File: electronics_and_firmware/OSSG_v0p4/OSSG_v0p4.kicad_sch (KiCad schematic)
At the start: 71 parts, among them IC1 DW01A, J1 USB_B_Micro, J2 External PDM Mic Input, Q1 FS8205A, Q2 Q_NPN_BEC, Q3 Q_NPN_BEC, Q4 Q_PMOS_GSD, SW1 SW_SPST, U1 ESP32-PICO-D4, U2 TP4056, U3 NCP167BMX330TBG, U4 CH9102F, U5 XC61CC3002MR, U6 MP23DB01HPTR

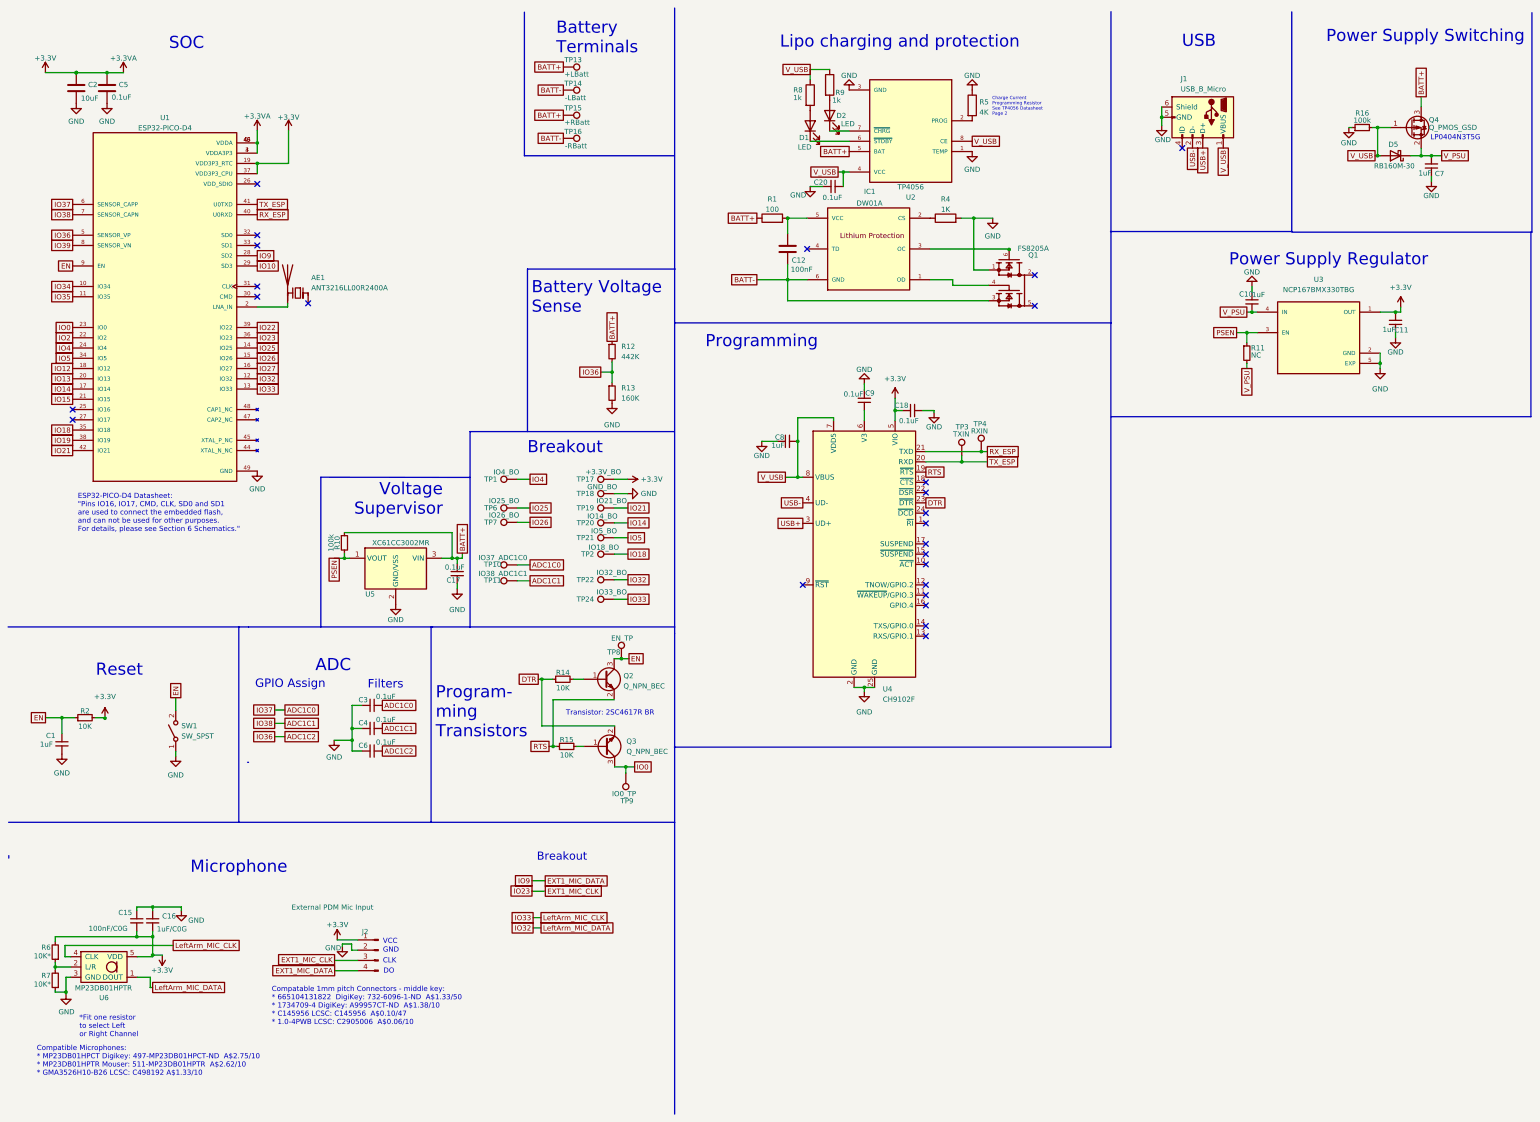
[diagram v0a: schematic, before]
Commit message: partial schematic update
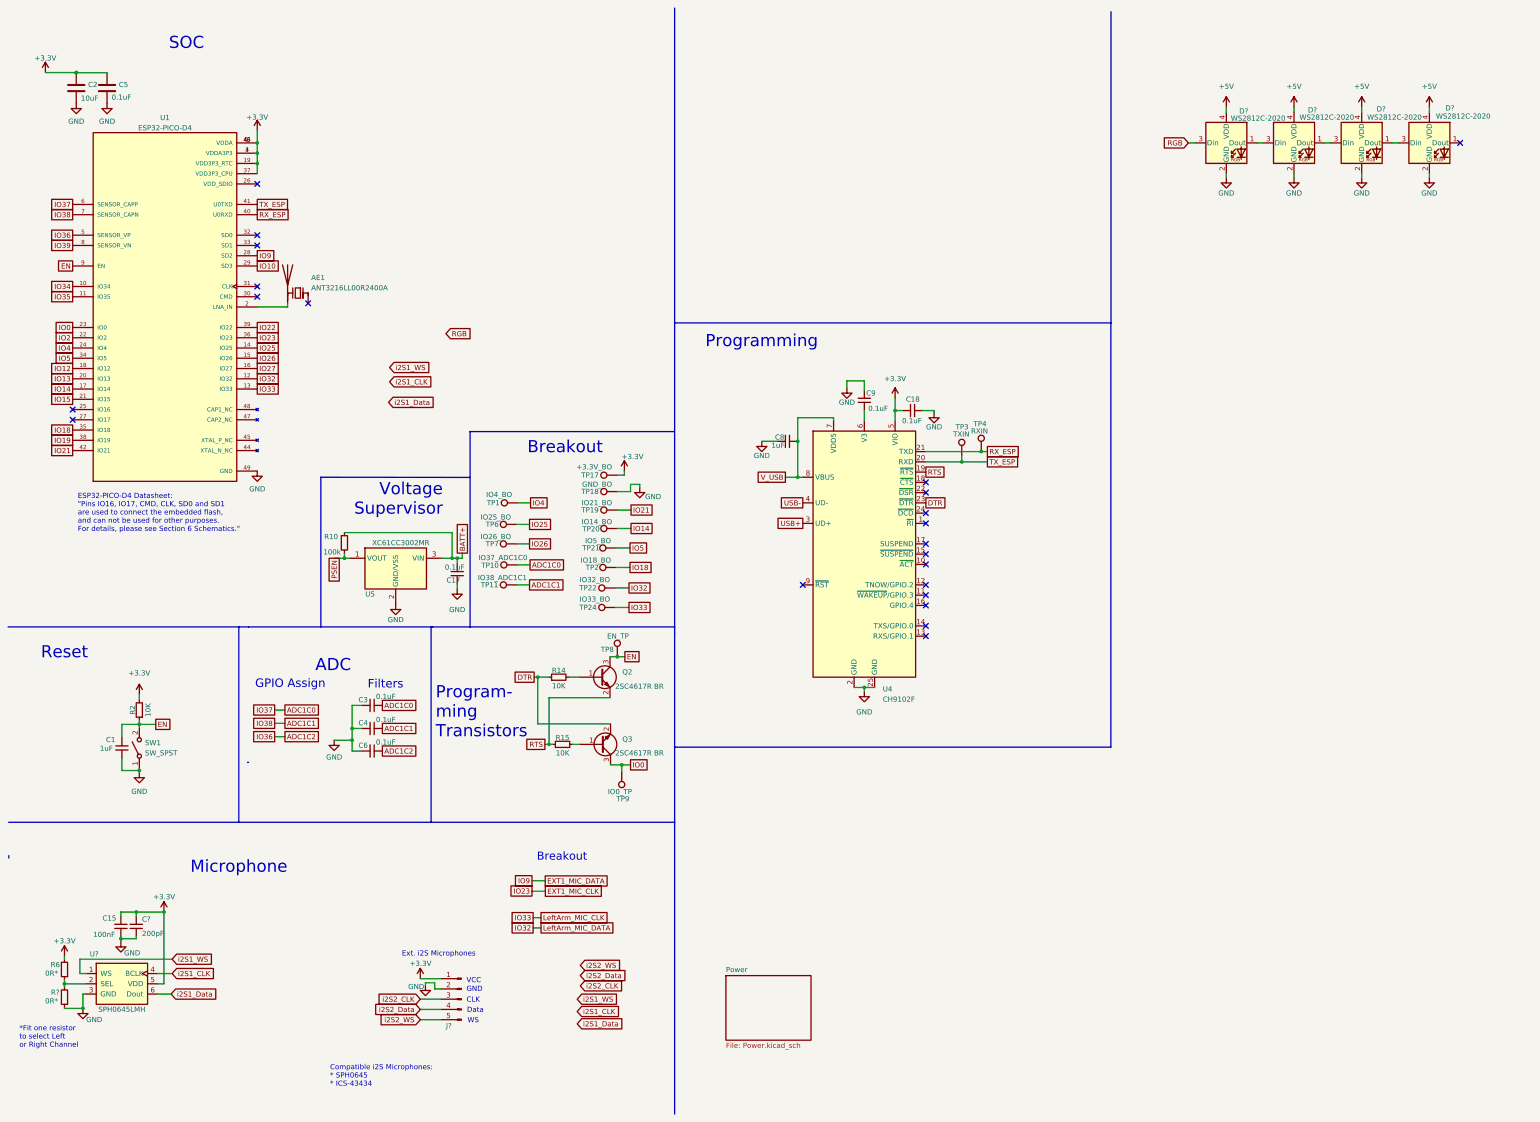
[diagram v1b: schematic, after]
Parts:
- removed C10, C11, C7: 1uF, Capacitor_SMD:C_0402_1005Metric, symbol Device:C_Small
- removed C12: 100nF, Capacitor_SMD:C_0402_1005Metric, symbol Device:C
- removed C16: 1uF/C0G, 1uF, symbol Device:C_Small
- removed C20: 0.1uF, Capacitor_SMD:C_0402_1005Metric, symbol Device:C_Small
- removed D1, D2: LED, Diode_SMD:D_0402_1005Metric, symbol Device:LED
- removed D5: RB160M-30, Diode_SMD:D_SOD-123, symbol Device:D_Schottky
- removed IC1: DW01A, Package_TO_SOT_SMD:SOT-23-6, symbol DW01A:DW01A
- removed J1: USB_B_Micro, Connector_USB:USB_Micro-B_Amphenol_10118194_Horizontal, symbol Connector:USB_B_Micro
- removed J2: External PDM Mic Input, OSSG_footprints:Solder-4P-Connector, symbol Connector:Conn_01x04_Male
- removed Q1: FS8205A, Package_TO_SOT_SMD:SOT-23-6, symbol FS8205A:FS8205A
- removed Q4: Q_PMOS_GSD, Package_TO_SOT_SMD:SOT-883, symbol Device:Q_PMOS_GSD
- removed R1: 100, Resistor_SMD:R_0402_1005Metric, symbol Device:R
- removed R11: NC, Resistor_SMD:R_0201_0603Metric, symbol Device:R_Small
- removed R12: 442K, Resistor_SMD:R_0402_1005Metric, symbol Device:R_Small
- removed R13: 160K, Resistor_SMD:R_0402_1005Metric, symbol Device:R_Small
- removed R16: 100k, Resistor_SMD:R_0402_1005Metric, symbol Device:R_Small
- removed R4: 1K, Resistor_SMD:R_0402_1005Metric, symbol Device:R
- removed R5: 4K, Resistor_SMD:R_0402_1005Metric, symbol Device:R
- removed R7: 10K*, Resistor_SMD:R_0402_1005Metric, symbol Device:R_Small
- removed R8, R9: 1k, Resistor_SMD:R_0402_1005Metric, symbol Device:R
- removed TP13: +LBatt, OSSG_footprints:Breakout_pads, symbol Connector:TestPoint
- removed TP14: -LBatt, OSSG_footprints:Breakout_pads, symbol Connector:TestPoint
- removed TP15: +RBatt, OSSG_footprints:Breakout_pads, symbol Connector:TestPoint
- removed TP16: -RBatt, OSSG_footprints:Breakout_pads, symbol Connector:TestPoint
- removed U2: TP4056, Package_SO:SOP-8_5.28x5.23mm_P1.27mm, symbol TP4056:TP4056
- removed U3: NCP167BMX330TBG, OSSG_footprints:REG_NCP167BMX330TBG, symbol NCP167BMX330TBG:NCP167BMX330TBG
- removed U6: MP23DB01HPTR, OSSG_footprints:MP23DB01HPTR, symbol microphone-rescue:MP23DB01HPTR-Pauls_Symbol_Library
- added C?: 200pF, Capacitor_SMD:C_0402_1005Metric, symbol Device:C_Small
- added D? (x4): WS2812C-2020, OSSG_footprints:LED_WS2812C-2020, symbol OSSG_components_lib:WS2812C-2020
- added J?: Conn_01x05_Male, symbol Connector:Conn_01x05_Male
- added R?: 0R*, Resistor_SMD:R_0402_1005Metric, symbol Device:R_Small
- added U?: SPH0645LMH, OSSG_footprints:SPH0645LM4H-B-SMD-GND, symbol OSSG_components_lib:SPH0645LMH
- C15: value 100nF/C0G -> 100nF
- Q2, Q3: value Q_NPN_BEC -> 2SC4617R BR
- R6: value 10K* -> 0R*
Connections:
- net +3V3: now also C15.1, U1.1 (VDDA), U1.3 (VDDA3P3), U1.4 (VDDA3P3), U1.43 (VDDA), U1.46 (VDDA), C?.2, J?.1 (Pin_1), U?.5 (VDD); no longer C15.2
- net GND: now also C15.2, C?.1, D?.2 (GND), D?.2 (GND), D?.2 (GND), D?.2 (GND), J?.2 (Pin_2), R?.1, U?.3 (GND); no longer C15.1
- net at R6.1: now also R?.2, U?.2 (SEL)
- removed net +3.3VA: C2.1, C5.1, U1.1 (VDDA), U1.3 (VDDA3P3), U1.4 (VDDA3P3), U1.43 (VDDA), U1.46 (VDDA)
- new net: D?.1 (Dout), D?.3 (Din) (x3)
- new net: C2.1, C5.1
- new net +5V: D?.4 (VDD), D?.4 (VDD), D?.4 (VDD), D?.4 (VDD)
- new net RGB: D?.3 (Din)
- new net i2S1_CLK: U?.4 (BCLK)
- new net i2S1_Data: U?.6 (Dout)
- new net i2S1_WS: U?.1 (WS)
- new net i2S2_CLK: J?.3 (Pin_3)
- new net i2S2_Data: J?.4 (Pin_4)
- new net i2S2_WS: J?.5 (Pin_5)
- no-connect marks 25 -> 22
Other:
- added sheet Power (Power.kicad_sch)
- note added: "Compatible i2S Microphones: * SPH0645 * ICS-43434"
- note added: "Data"
- note added: "Ext. i2S Microphones"
- note added: "WS"
- note removed: "Battery Terminals"
- note removed: "Battery Voltage Sense"
- note removed: "Charge Current Programming Resistor See TP4056 Datasheet Page 2"
- note removed: "Compatable 1mm pitch Connectors - middle key: * 665104131822 DigiKey: 732-6096-1-ND A$1.33/50 * 1734709-4 DigiKey: A99957CT-ND A$1.38/10 * C145956 LCSC: C145956 A$0.10/47 * 1.0-4PWB LCSC: C2905006 A$0.06/10"
- note removed: "Compatible Microphones: * MP23DB01HPCT Digikey: 497-MP23DB01HPCT-ND A$2.75/10 * MP23DB01HPTR Mouser: 511-MP23DB01HPTR A$2.62/10 * GMA3526H10-B26 LCSC: C498192 A$1.33/10"
- note removed: "DO"
- note removed: "LP0404N3T5G"
- note removed: "Lipo charging and protection"
- note removed: "Power Supply Regulator"
- note removed: "Power Supply Switching"
- note removed: "Transistor: 2SC4617R BR"
- note removed: "USB"
- title: Open Source Smart Glasses v0.3 -> Open Source Smart Glasses v0.4
- moved on the sheet: C1, C15, Q2, Q3, R14, R15, R2, R6, SW1, TP1, TP11, TP17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

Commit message: filled out MP2615 circuit
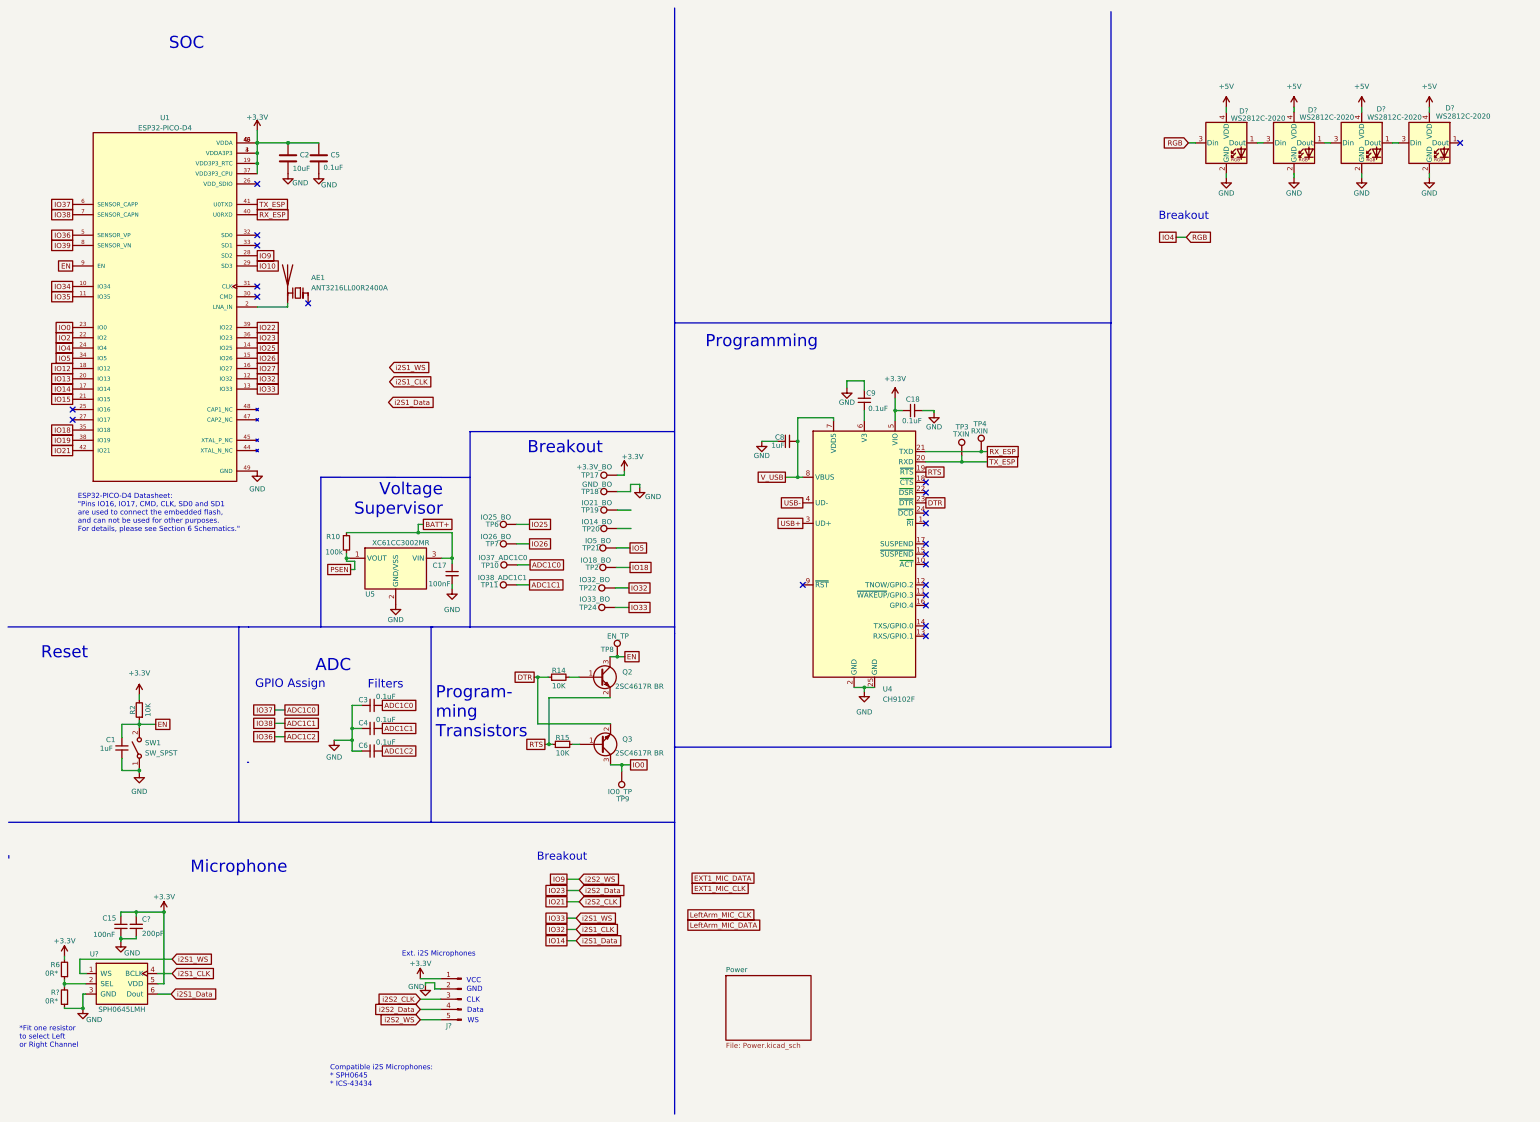
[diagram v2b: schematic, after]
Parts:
- removed TP1: IO4_BO, OSSG_footprints:Breakout_pads_small, symbol Connector:TestPoint
- C17: value 0.1uF -> 100nF
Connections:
- net RGB is gone; now on net IO4: D?.3 (Din)
- net i2S1_CLK is gone; now on net IO32: U?.4 (BCLK)
- net i2S1_Data is gone; now on net IO14: U?.6 (Dout)
- net i2S1_WS is gone; now on net IO33: U?.1 (WS)
- net i2S2_CLK is gone; now on net IO21: J?.3 (Pin_3)
- net EXT1_MIC_CLK: no longer U1.36 (IO23)
- net EXT1_MIC_DATA: no longer U1.28 (SD2)
- net IO14: no longer TP20.1
- net IO21: no longer TP19.1
- net i2S2_Data renamed IO23
- net IO23: now also U1.36 (IO23)
- net i2S2_WS renamed IO9
- net IO9: now also U1.28 (SD2)
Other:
- moved on the sheet: C17, C2, C5, R10

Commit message: about to change power switching MOSFETs
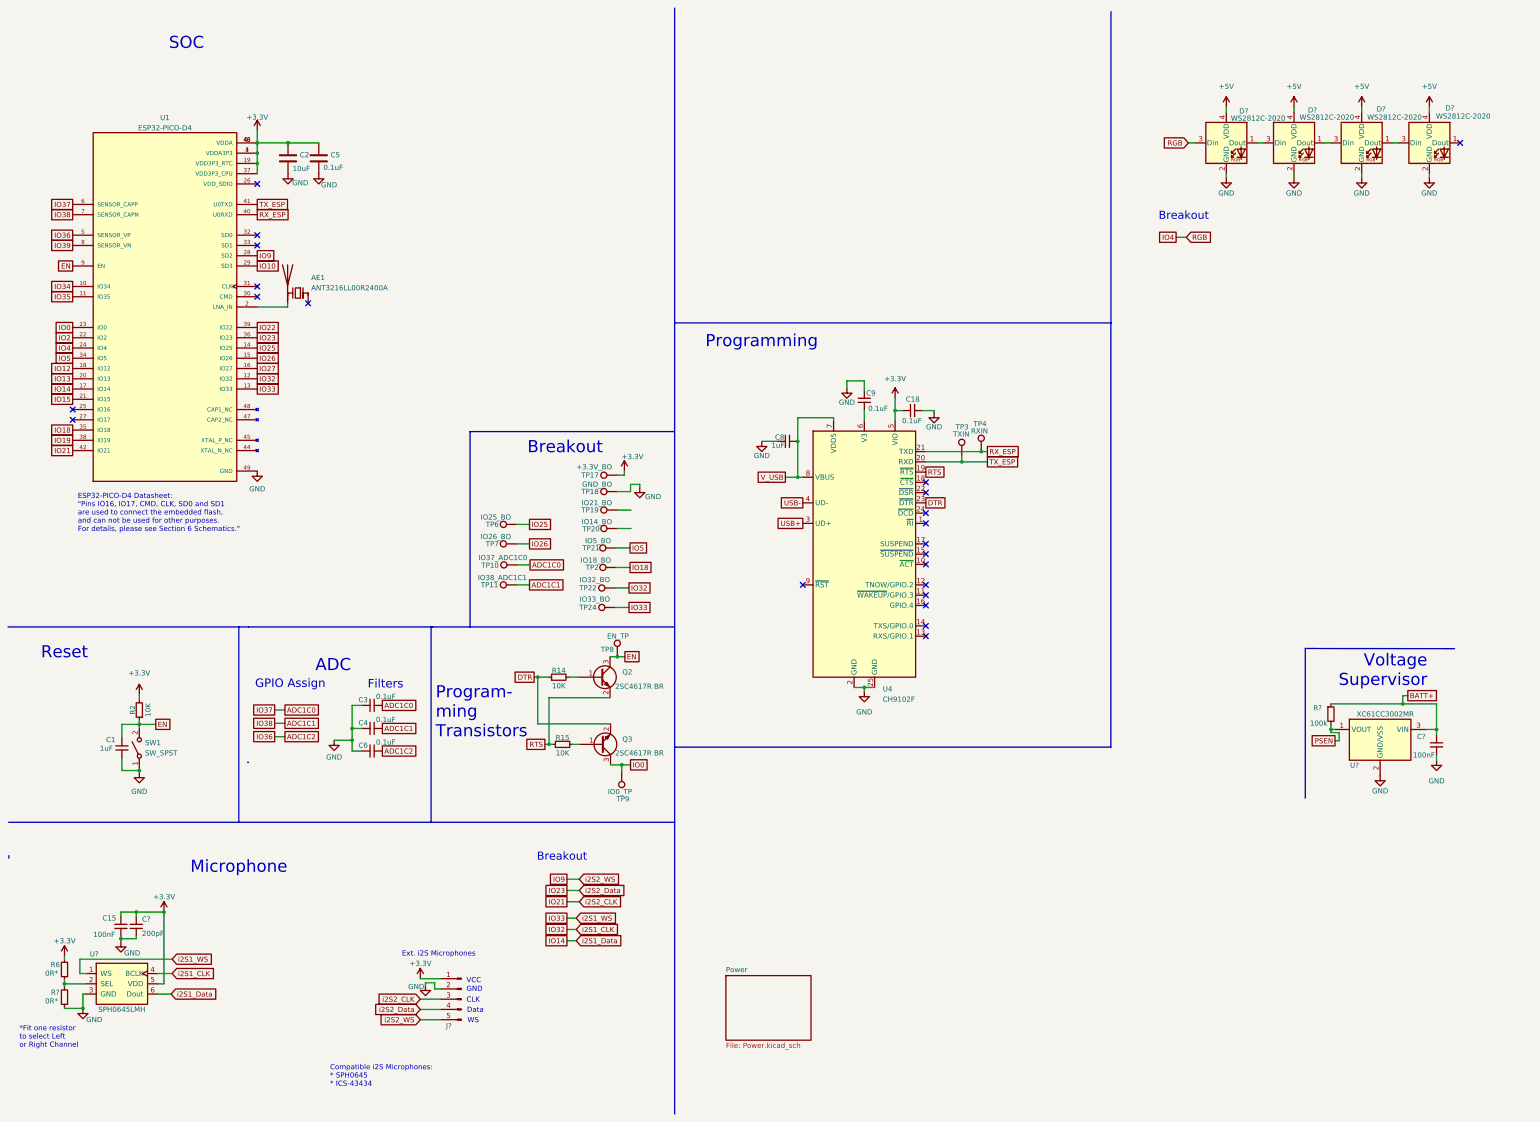
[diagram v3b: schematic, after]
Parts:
- removed C17: 100nF, Capacitor_SMD:C_0402_1005Metric, symbol Device:C_Small
- removed R10: 100k, Resistor_SMD:R_0402_1005Metric, symbol Device:R_Small
- removed U5: XC61CC3002MR, Package_TO_SOT_SMD:SOT-23, symbol OSSG_components_lib:XC61C_voltage_supervisor
- added C?: 100nF, Capacitor_SMD:C_0402_1005Metric, symbol Device:C_Small
- added R?: 100k, Resistor_SMD:R_0402_1005Metric, symbol Device:R_Small
- added U?: XC61CC3002MR, Package_TO_SOT_SMD:SOT-23, symbol OSSG_components_lib:XC61C_voltage_supervisor
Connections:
- net BATT+: now also C?.1, R?.1, U?.3 (VIN)
- net GND: now also C?.2, U?.2 (GND/VSS)
- net PSEN: now also R?.2, U?.1 (VOUT)

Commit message: V0.4.1 schematic
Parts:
- removed C?: 100nF, Capacitor_SMD:C_0402_1005Metric, symbol Device:C_Small
- removed R?: 100k, Resistor_SMD:R_0402_1005Metric, symbol Device:R_Small
- removed TP19: IO21_BO, OSSG_footprints:Breakout_pads_small, symbol Connector:TestPoint
- removed TP20: IO14_BO, OSSG_footprints:Breakout_pads_small, symbol Connector:TestPoint
- removed U?: XC61CC3002MR, Package_TO_SOT_SMD:SOT-23, symbol OSSG_components_lib:XC61C_voltage_supervisor
- J1: renamed from J?; footprint (none) -> Connector_PinHeader_1.00mm:PinHeader_1x05_P1.00mm_Horizontal
- gave numbers to parts that had none: 7
- renumbered C15 to C1, C9 to C10, C18 to C11, C1 to C2, C2 to C4, C3 to C6, C4 to C7, C6 to C8, C8 to C9, Q2 to Q1, Q3 to Q2, R6 to R1, R2 to R3, R14 to R4, R15 to R5, TP6 to TP1, TP21 to TP10, TP2 to TP11, TP9 to TP12, TP3 to TP13, TP4 to TP14, TP7 to TP2, TP11 to TP3, TP10 to TP4, TP8 to TP5, TP22 to TP6, TP24 to TP7, TP17 to TP8, TP18 to TP9, U1 to U2, U4 to U3
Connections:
- net IO10: no longer names the net of U2.29 (SD3)
- no-connect marks 22 -> 23
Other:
- note added: "ESP32-PICO-D4 Datasheet: "Pins IO16, IO17, CMD, CLK, SD0, SD1 and SD13 (25, 26, 30, 31, 32, 33, 29) are used to connect the embedded flash, and can not be used for other purposes. For details, please see Section 6 Schematics.""
- note added: "Filter Caps should be placed close to MCU"
- note added: "Input only: IO34, IP35, IO36, IO37, IO38, IO39 10, 11, 5, 6, 7, 8"
- note added: "Programming Transistors"
- note added: "Strapping Pins: GPIO0, IO2, IO5, IO12, IO15"
- note removed: "ESP32-PICO-D4 Datasheet: "Pins IO16, IO17, CMD, CLK, SD0 and SD1 are used to connect the embedded flash, and can not be used for other purposes. For details, please see Section 6 Schematics.""
- note removed: "Program- ming Transistors"
- note removed: "Voltage Supervisor"
- moved on the sheet: AE1, Q1, Q2, R4, R5, TP1, TP10, TP11, TP12, TP2, TP3, TP4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
